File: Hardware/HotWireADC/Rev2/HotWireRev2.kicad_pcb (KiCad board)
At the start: 2 copper layers, 48 parts, among them CON1 BARREL_JACK, P1 BNC, P2 BNC, P3 BNC, P4 BNC, P5 CONN_02X06, SW1 SW_PUSH_SMALL, U1 OPA320, U2 OPA320, U3 OPA320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

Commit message: moved external reference to BNC connector & tidied layout
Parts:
- added P6: BNC, Connect:bnc-ci, F.Cu at (24.7, 56.9)
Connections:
- P5 pad 8: EXT_REF -> (no net)
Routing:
- net EXT_REF: track 0.00 -> 30.9 mm
- net GNDA: track 542.6 -> 566.3 mm
- net Net-(R1-Pad2): track 3.21 -> 6.69 mm
- net Net-(R3-Pad2): track 2.43 -> 5.90 mm
- net Net-(R2-Pad2): track 3.51 -> 6.80 mm
- net Net-(R4-Pad2): track 2.74 -> 6.04 mm
- added copper zone on F.Cu, net GNDA
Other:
- board outline added: 87 x 109.9 mm

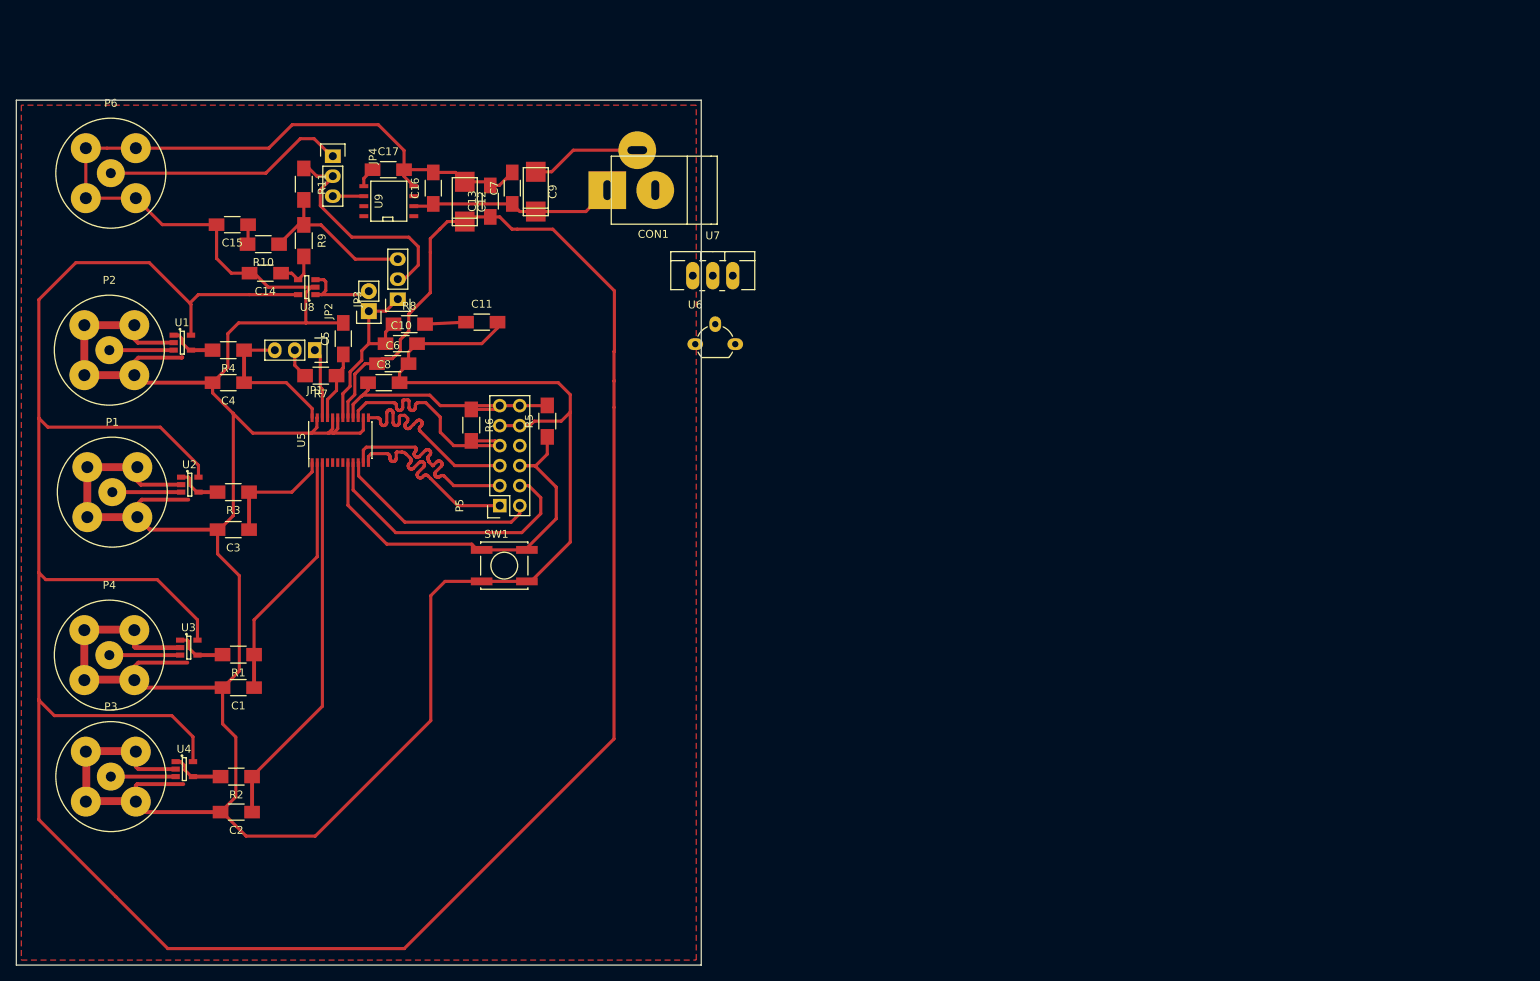
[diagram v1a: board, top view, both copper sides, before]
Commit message: updated regulator footprint and removed additional regulator
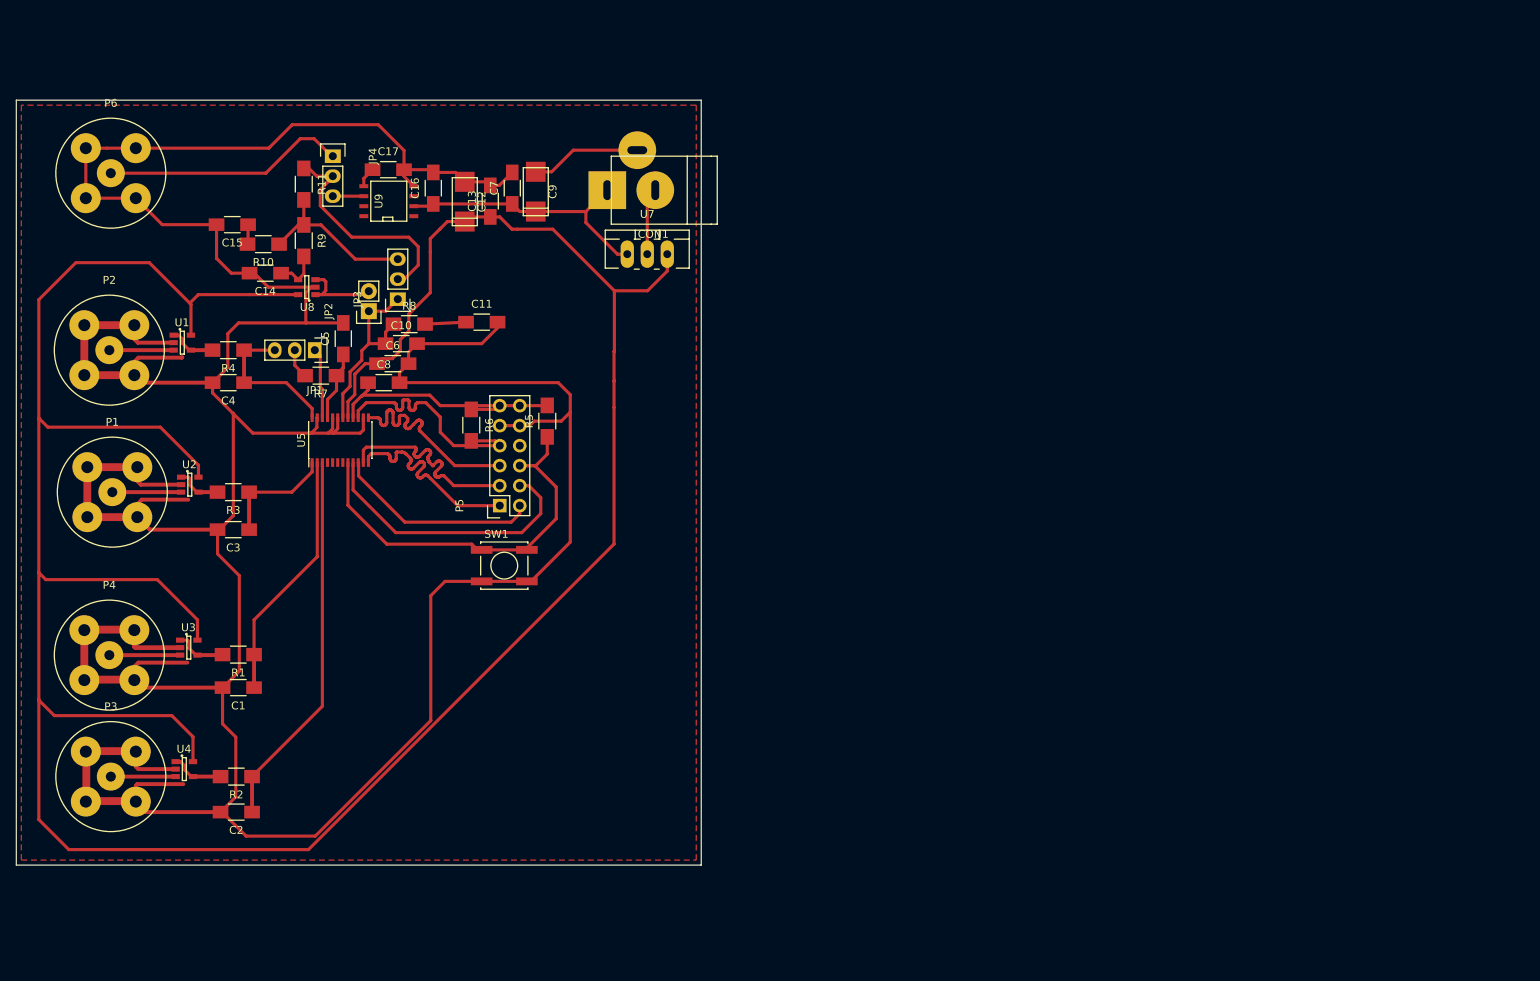
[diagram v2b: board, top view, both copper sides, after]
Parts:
- removed U6: TL750L05, TO_SOT_Packages_THT:TO-92_Molded_Wide_Oval
- U7: footprint TO_SOT_Packages_THT:TO-220_Neutral123_Vertical_LargePads -> CustomFootprints:TO-220_REGULATORVIGNDVO_Vertical_LargePads
- moved U7 8.76 mm to (92.8, 67.2)
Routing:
- net +5VA: track 386.8 -> 371.8 mm
- net GNDA: track 566.3 -> 574.9 mm
- net VCC: track 26.2 -> 34.5 mm
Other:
- board size 87 x 109.9 mm -> 87 x 97.2 mm

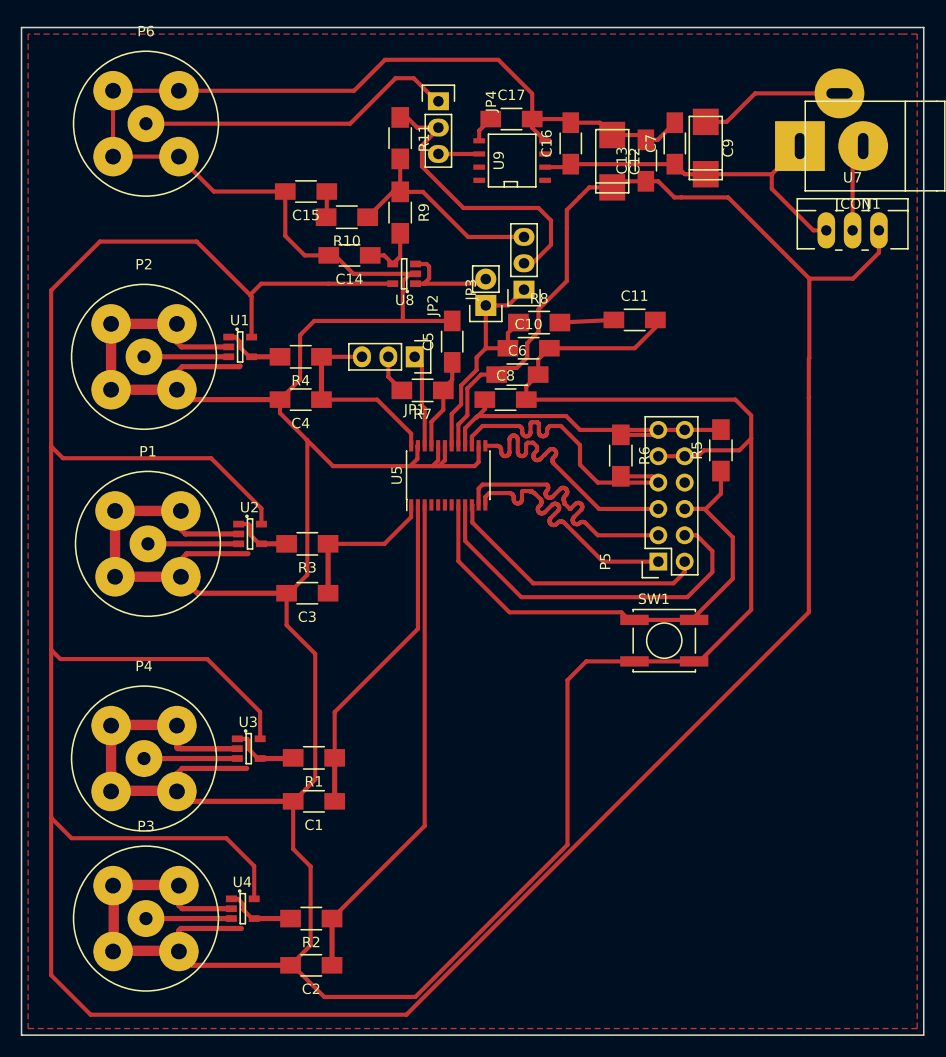
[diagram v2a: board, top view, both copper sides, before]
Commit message: increased track widths.
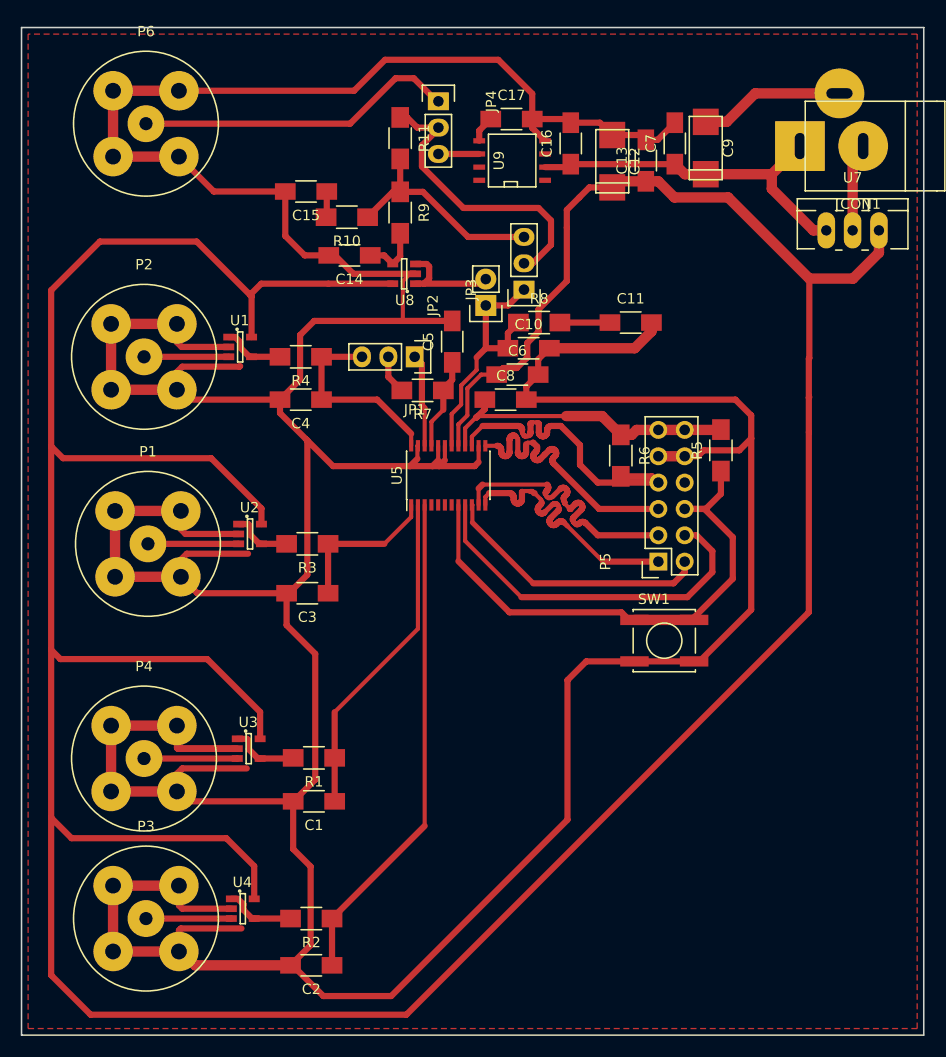
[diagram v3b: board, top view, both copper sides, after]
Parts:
- moved C11 0.46 mm to (71.4, 76.1)
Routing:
- net GNDA: track 574.9 -> 641.1 mm
- net VCC: track 34.5 -> 46.8 mm
- net +5VA: track 371.8 -> 381.6 mm
- net +3V3: track 33.3 -> 29.9 mm
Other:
- net class Default: trace_width 0.4 -> 0.6

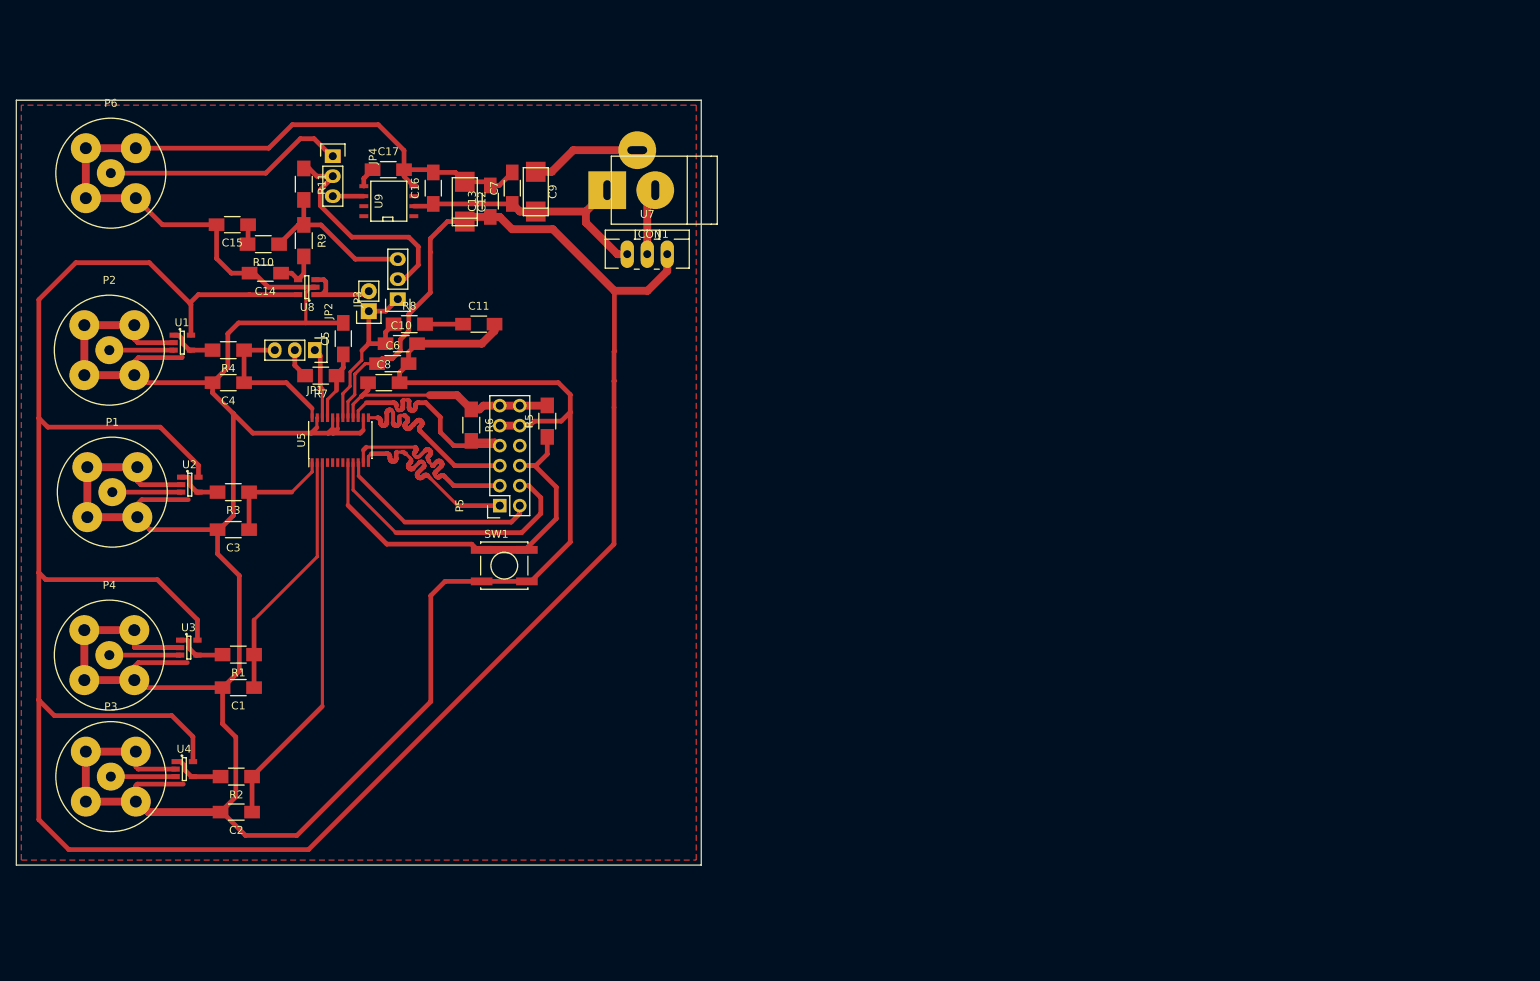
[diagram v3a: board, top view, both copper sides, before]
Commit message: tidied layout added text to silk added mounting holes and alignment marks
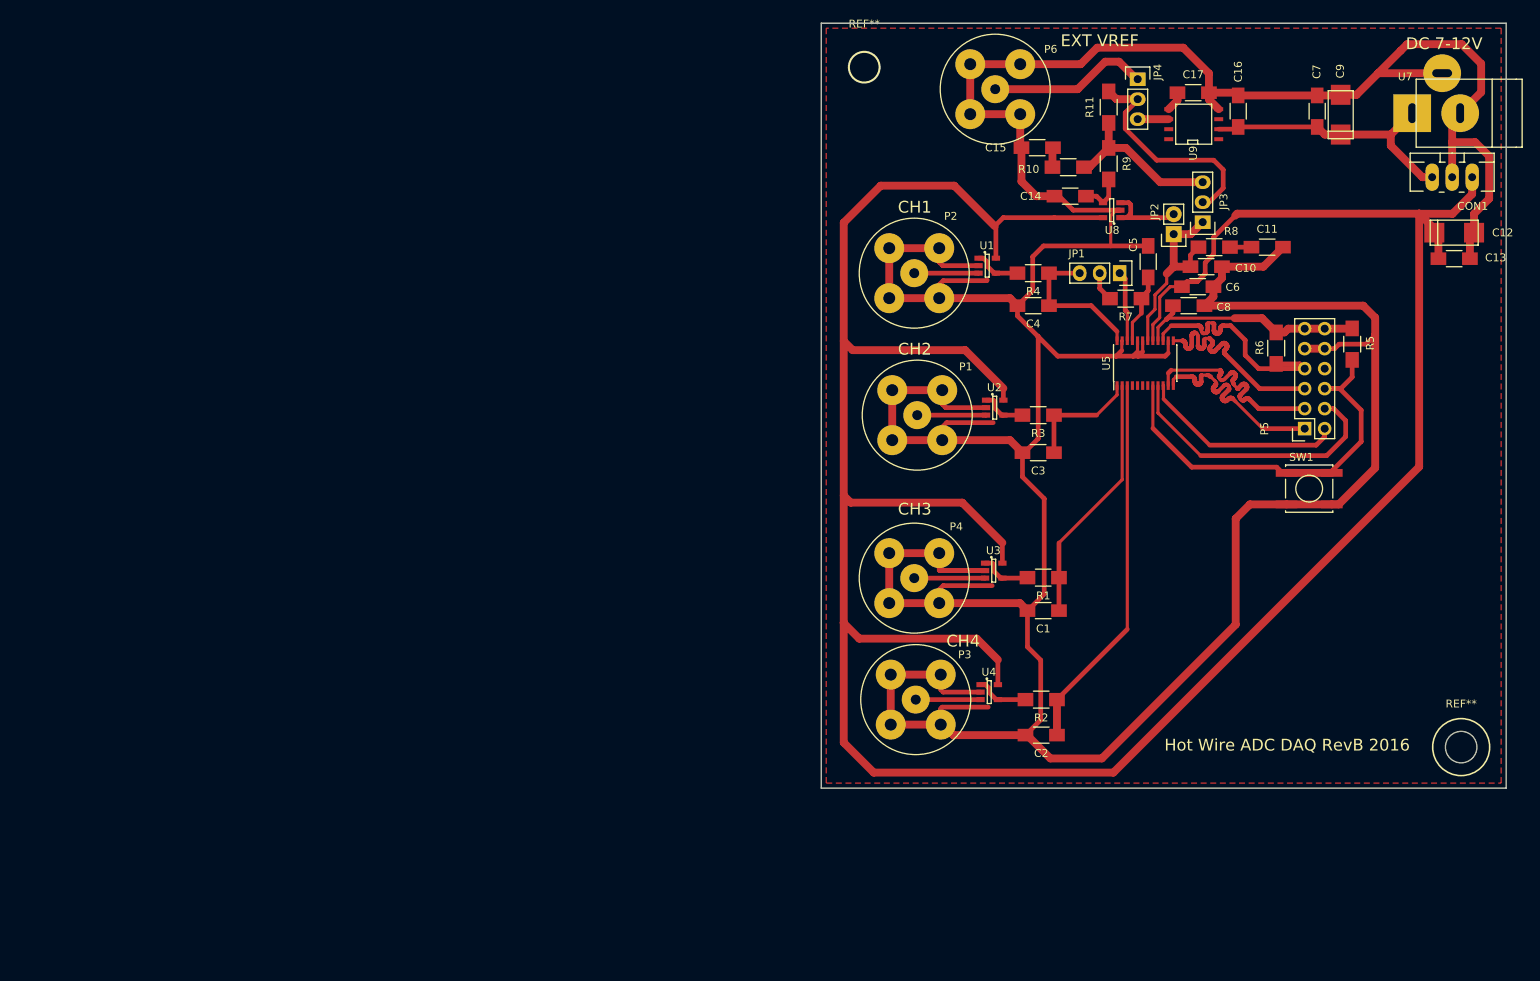
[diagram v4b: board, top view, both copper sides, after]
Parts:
- added REF**: MountingHole_4mm, Mounting_Holes:MountingHole_4mm, F.Cu at (120.4, 43.4)
- added REF**: MountingHole_4mm, Mounting_Holes:MountingHole_4mm, F.Cu at (196.2, 129.8)
- moved C12 125.7 mm to (195.3, 64.5), turned to 180 degrees
- moved C13 122.6 mm to (195.3, 67.8), turned to 0 degrees
- moved P6 112.8 mm to (137.0, 46.2)
- moved C10 102.7 mm to (163.8, 68.8)
- moved C4 102.7 mm to (141.9, 73.7)
- moved JP1 102.7 mm to (152.8, 69.6)
- moved JP3 102.7 mm to (163.4, 63.1)
- moved JP4 102.7 mm to (155.1, 45.0)
- moved R4 102.7 mm to (141.9, 69.6)
- moved R5 102.7 mm to (182.4, 78.6)
- moved R7 102.7 mm to (153.6, 72.8)
- moved R8 102.7 mm to (164.8, 66.3)
- moved U2 102.7 mm to (137.0, 86.7)
- moved U9 102.7 mm to (162.2, 50.7)
- moved C16 102.7 mm to (167.9, 49.0)
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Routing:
- net +5VA: track 381.6 -> 650.8 mm
- net GNDA: track 641.1 -> 653.7 mm
- net EXT_REF: track 30.9 -> 20.5 mm
- net Net-(C11-Pad1): track 4.83 -> 2.73 mm
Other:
- rule trace_min: 0.2 -> 0.4
- board text added: "CH1"
- board text added: "CH2"
- board text added: "CH3"
- board text added: "CH4"
- board text added: "DC 7-12V"
- board text added: "EXT VREF"
- board text added: "Hot Wire ADC DAQ RevB 2016"
